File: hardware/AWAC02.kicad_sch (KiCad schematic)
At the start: 14 parts, among them J1 Barrel_Jack, U1 ATmega328-P, U2 MCP7940M, U3 L7805, Y1 32.768kHz

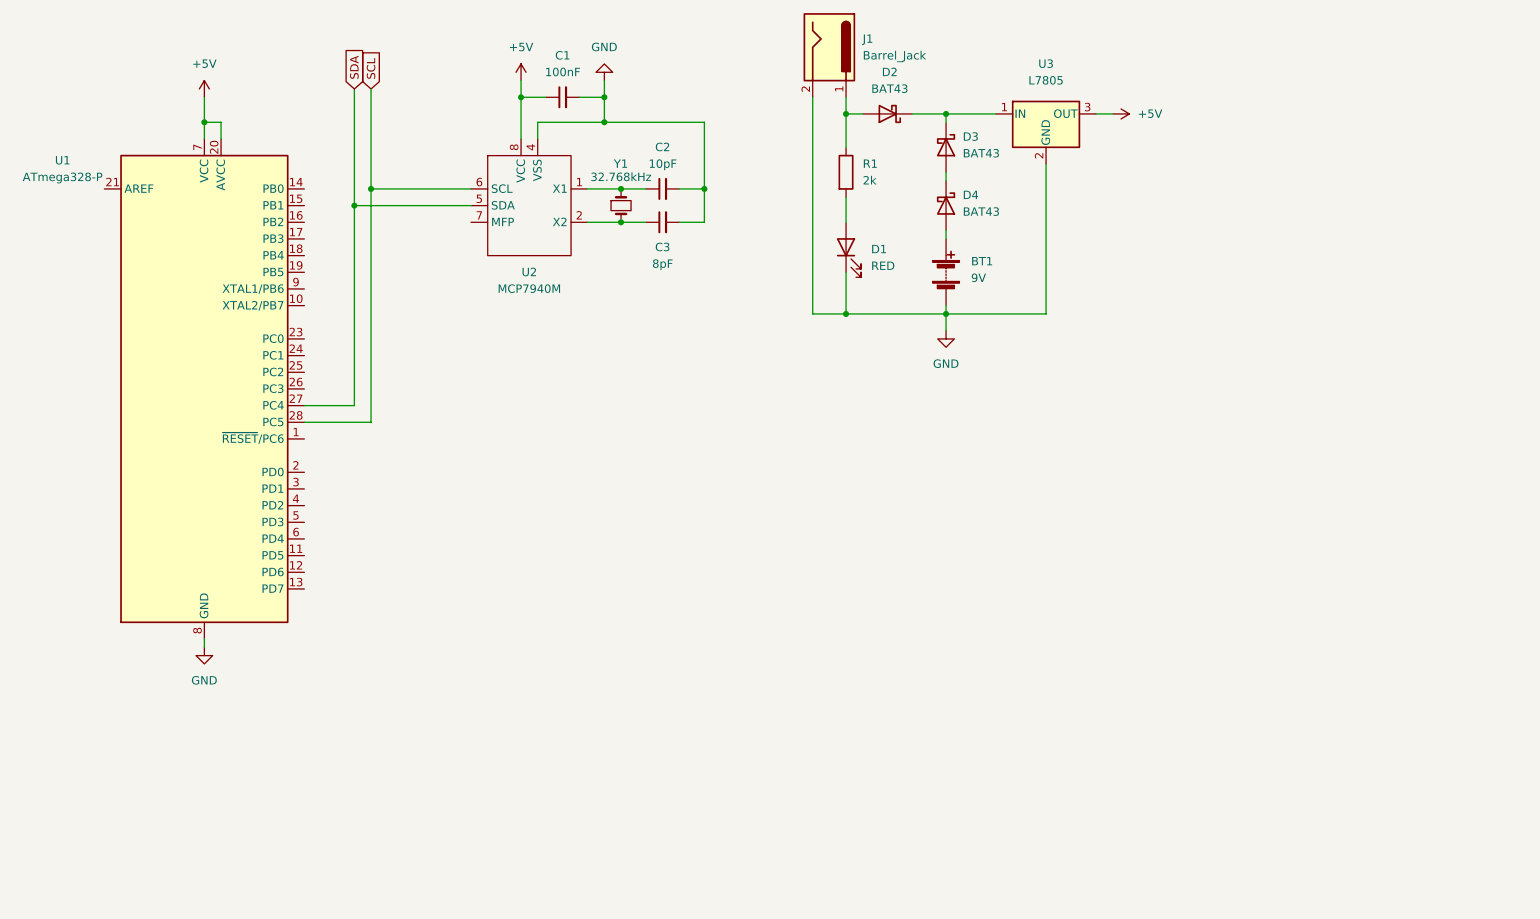
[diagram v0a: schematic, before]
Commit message: Add push buttons to schematic
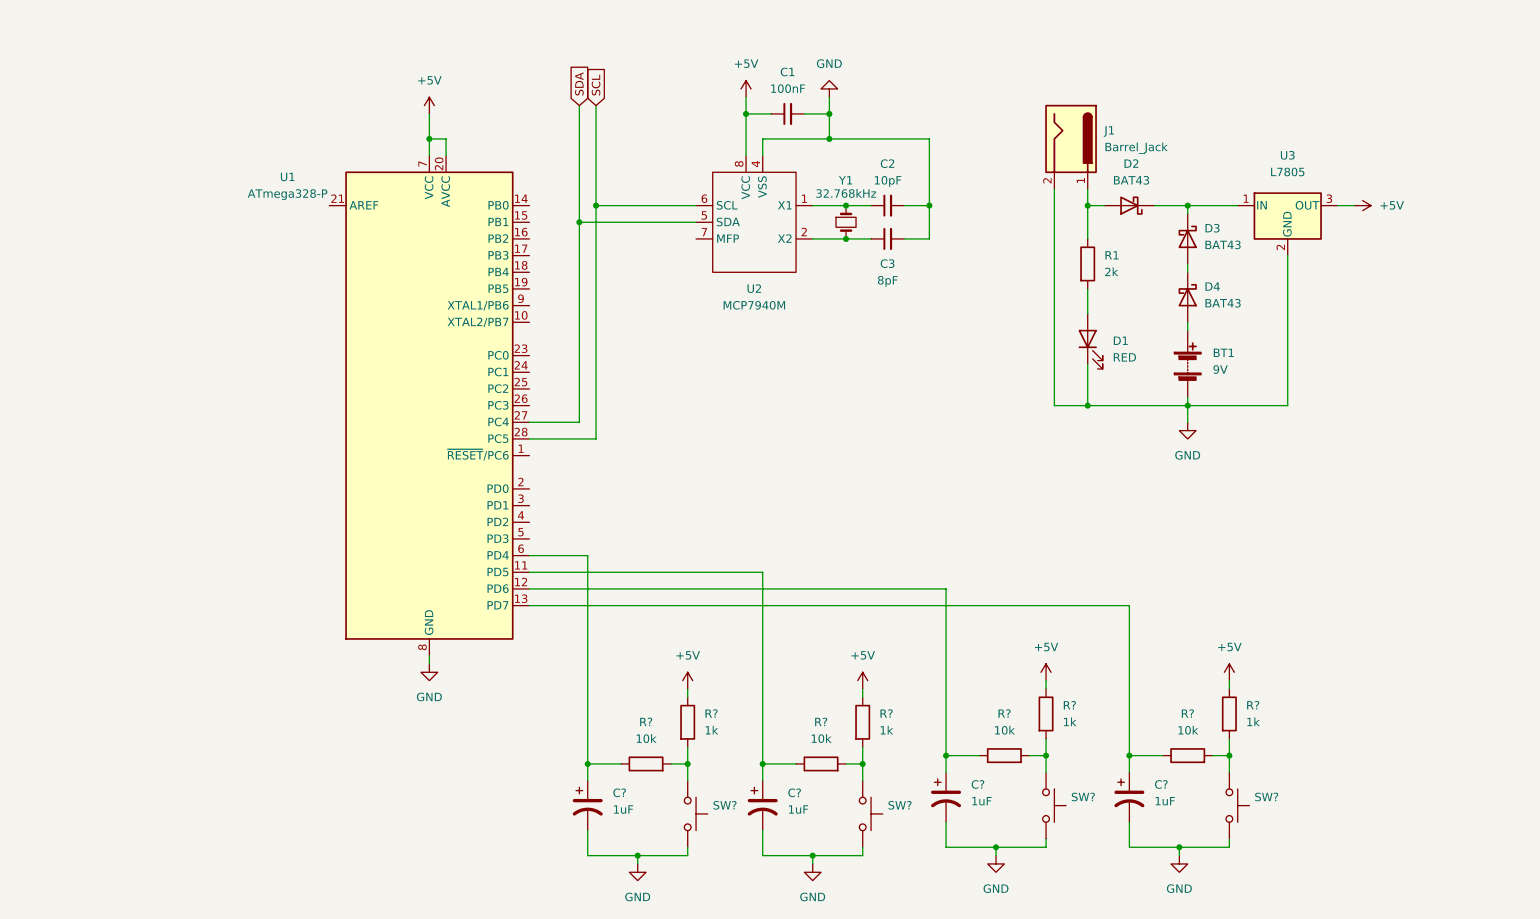
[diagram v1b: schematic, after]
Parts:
- added C? (x4): 1uF, symbol Device:C_Polarized_US
- added R? (x4): 10k, symbol Device:R
- added R? (x4): 1k, symbol Device:R
- added SW? (x4): (no value), symbol Switch:SW_Push
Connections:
- net +5V: now also R?.1, R?.1, R?.1, R?.1
- net GND: now also C?.2, C?.2, C?.2, C?.2, SW?.2, SW?.2, SW?.2, SW?.2
- net at U1.11 (PD5): now also C?.1, R?.1
- net at U1.12 (PD6): now also C?.1, R?.1
- net at U1.13 (PD7): now also C?.1, R?.1
- net at U1.6 (PD4): now also C?.1, R?.1
- new net: R?.2, R?.2, SW?.1 (x4)
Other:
- moved on the sheet: BT1, C1, C2, C3, D1, D2, D3, D4, J1, R1, U1, U2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

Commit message: Update circuit
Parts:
- removed C?: 1uF, symbol Device:C_Polarized_US
- removed R?: 10k, symbol Device:R
- removed R?: 1k, symbol Device:R
- removed SW?: (no value), symbol Switch:SW_Push
- added C?: 47uF, symbol Device:C_Polarized_US
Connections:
- net +5V: now also C?.1
- net GND: now also C?.2
- net at U1.6 (PD4): now also U2.7 (MFP)
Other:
- moved on the sheet: C?, R?, SW?

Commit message: Update schematics
- Add MFP pullup resistor
- Add buzzer
- Add buzzer led
- Change power in
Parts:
- removed D4: BAT43, Diode_THT:D_DO-35_SOD27_P7.62mm_Horizontal, symbol Diode:BAT43
- added BZ?: Buzzer, symbol Device:Buzzer
- added D?: RED, symbol Device:LED
- added R?: 10k, symbol Device:R
- added R?: 2k, symbol Device:R
- gave numbers to parts that had none: 13
- renumbered C1 to C2, C2 to C3, C3 to C4, R1 to R5
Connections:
- net +5V: now also R?.1
- net GND: now also BZ?.2 (+), D?.1 (K); no longer D1.1 (K)
- net at D3.2 (A): now also BT1.1 (+)
- net at D2.2 (A), J1.1: no longer R5.1
- net at U1.6 (PD4), U2.7 (MFP): now also R?.2
- net at U1.23 (PC0): now also BZ?.1 (-), R?.1
- new net: D?.2 (A), R?.2
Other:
- moved on the sheet: BT1, C7, D1, D2, D3, J1, R5, U3

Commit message: Update schematic
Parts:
- removed D1: RED, symbol Device:LED
- removed R5: 2k, symbol Device:R
- added C1: 100nF, symbol Device:C_Small
- gave numbers to parts that had none: 4
- renumbered C1 to C2, C2 to C3, C3 to C4, C4 to C5, C5 to C6, C6 to C7, C7 to C8, D2 to D1, D3 to D2, R1 to R2, R2 to R3, R3 to R4, R4 to R5
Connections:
- net +5V: now also C1.2
- net GND: now also C1.1
